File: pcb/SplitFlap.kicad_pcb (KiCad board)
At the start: 2 copper layers, 35 x 35 mm, 21 parts, among them J1 A1_3, U1 PCF8575DBR, U2 ULN2003

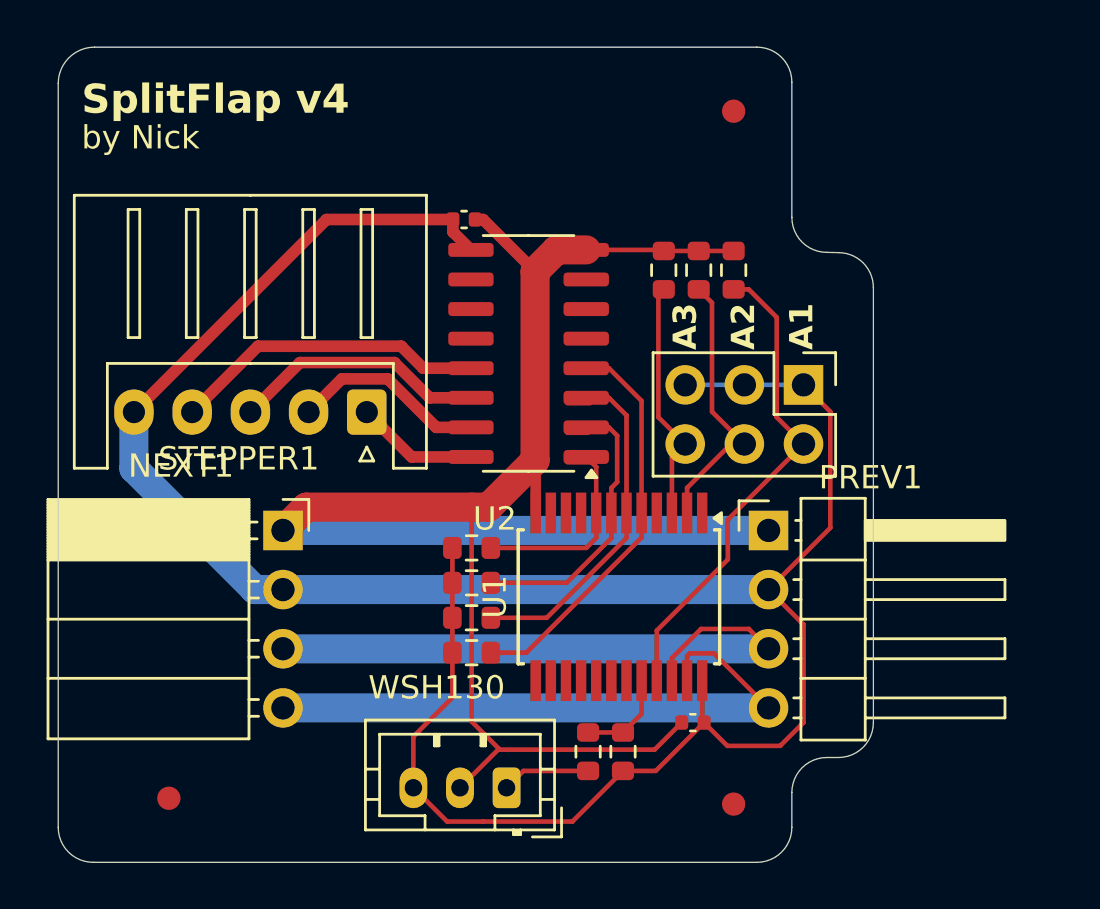
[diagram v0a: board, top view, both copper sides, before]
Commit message: Add optional data lines pull-up
Required as the ESP32 by default does not pull up the data lines to
5v.  Should only be activated once per circuit (display).
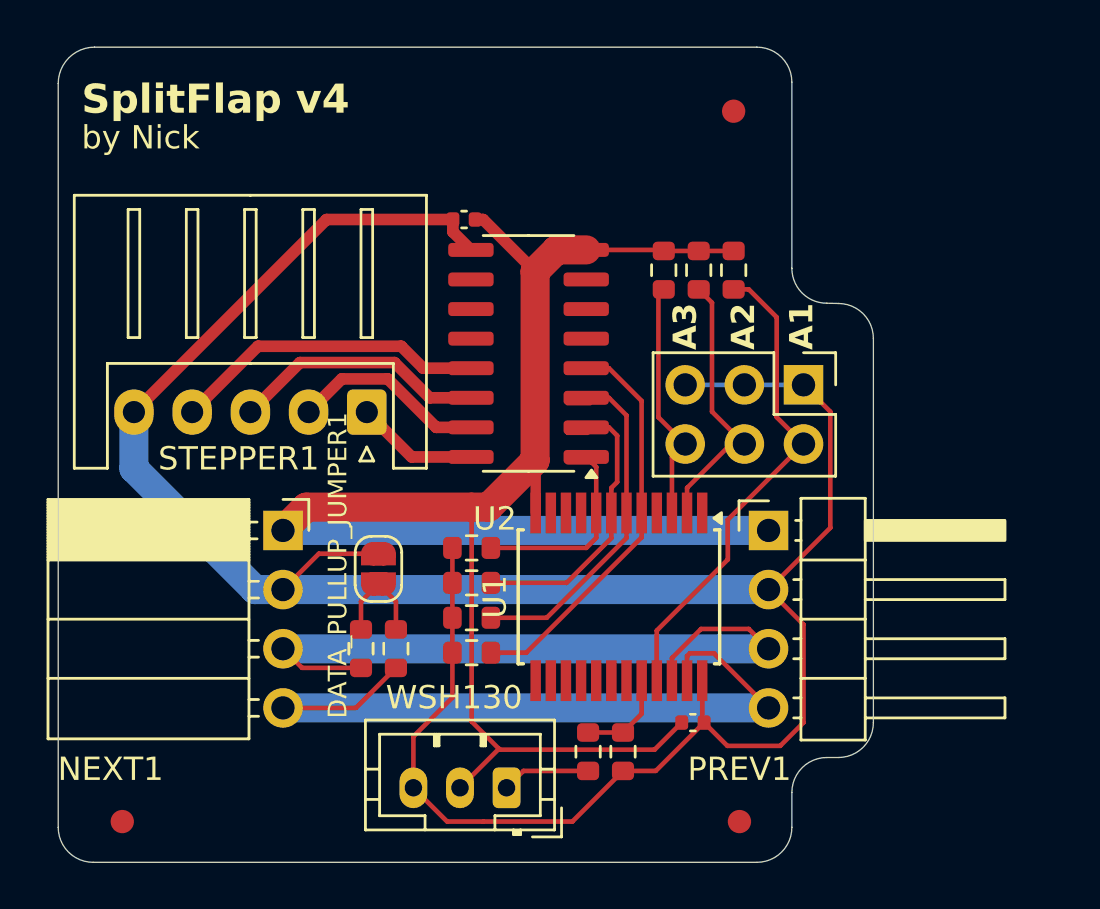
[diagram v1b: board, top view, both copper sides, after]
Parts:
- added DATA_PULLUP_JUMPER1: SolderJumper_2_Open, Jumper:SolderJumper-2_P1.3mm_Open_RoundedPad1.0x1.5mm, F.Cu at (158.8, 81.9)
- added SCL_PULL_UP1: 4K7, Resistor_SMD:R_0603_1608Metric, F.Cu at (158.0, 85.3)
- added SDA_PULL_UP1: 4K7, Resistor_SMD:R_0603_1608Metric, F.Cu at (159.5, 85.3)
- moved REF** 2.24 mm to (147.8, 92.8)
- moved REF** 0.79 mm to (174.2, 92.8)
- renumbered C1 to C1_BYPASS1
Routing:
- net Net-(NEXT1-Pin_4): track 26.4 -> 32.0 mm
- net +5V: track 105.1 -> 109.9 mm
- net Net-(DATA_PULLUP_JUMPER1-B): track 0.00 -> 4.52 mm
- net Net-(NEXT1-Pin_3): track 26.8 -> 30.5 mm
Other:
- outline, holes or cut-outs redrawn

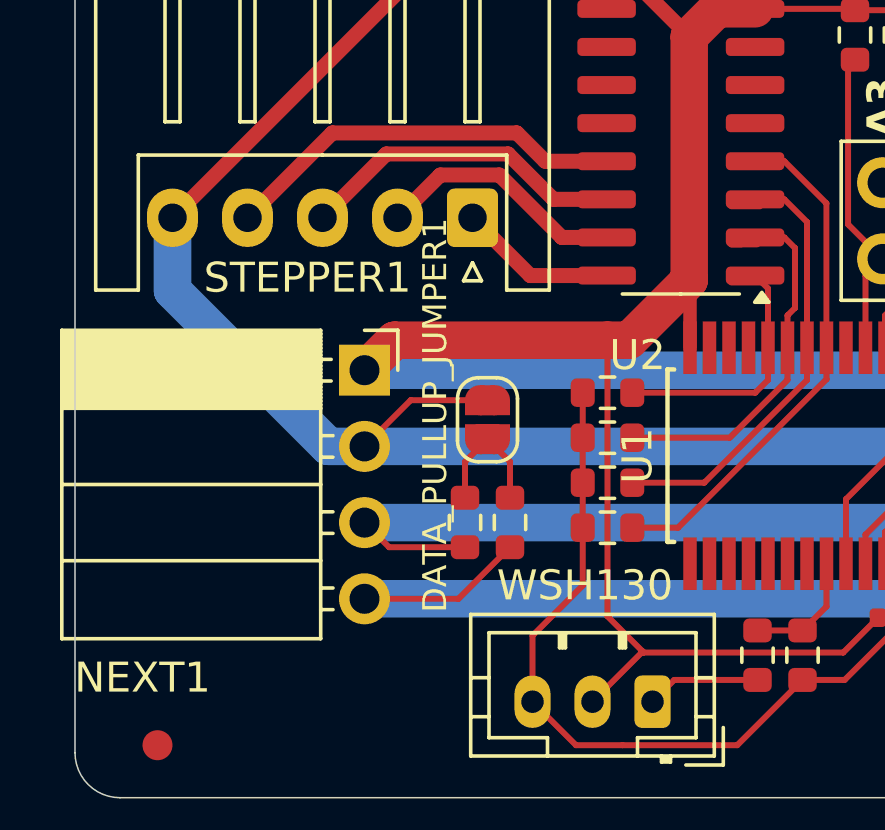
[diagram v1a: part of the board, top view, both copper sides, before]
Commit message: Rename pull-up jumper
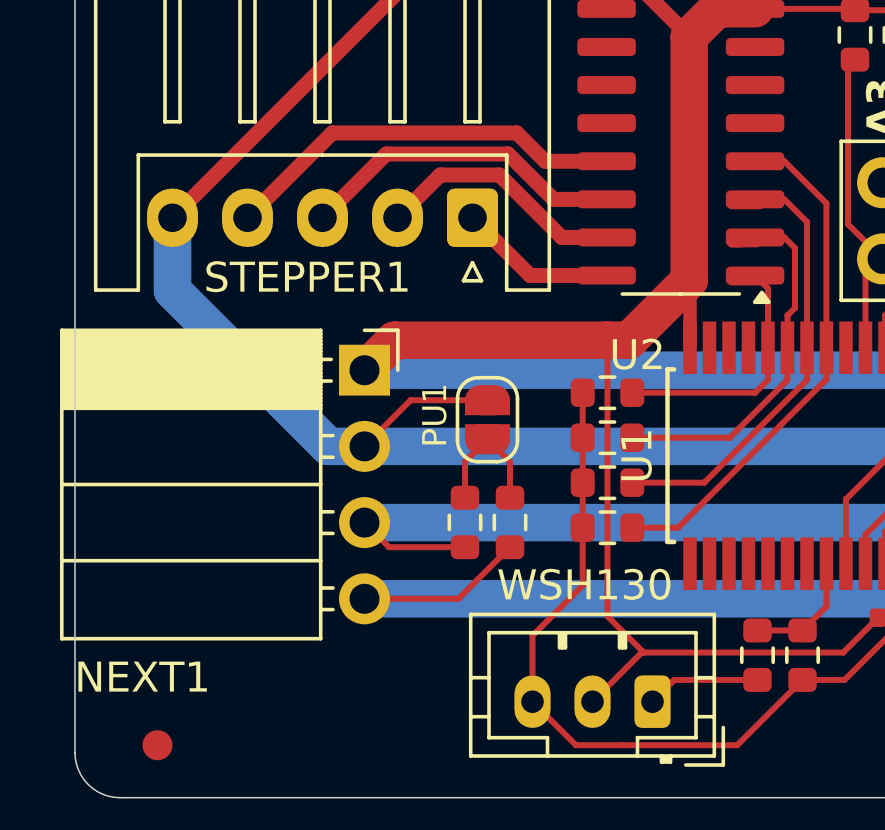
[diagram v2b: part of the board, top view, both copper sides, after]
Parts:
- renumbered DATA_PULLUP_JUMPER1 to PU1
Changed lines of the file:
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@@
 		(descr "SMD Solder Jumper, 1x1.5mm, rounded Pads, 0.3mm gap, open")
 		(tags "solder jumper open")
-		(property "Reference" "DATA_PULLUP_JUMPER1"
+		(property "Reference" "PU1"
 			(at -0.15 1.75 90)
 			(layer "F.SilkS")

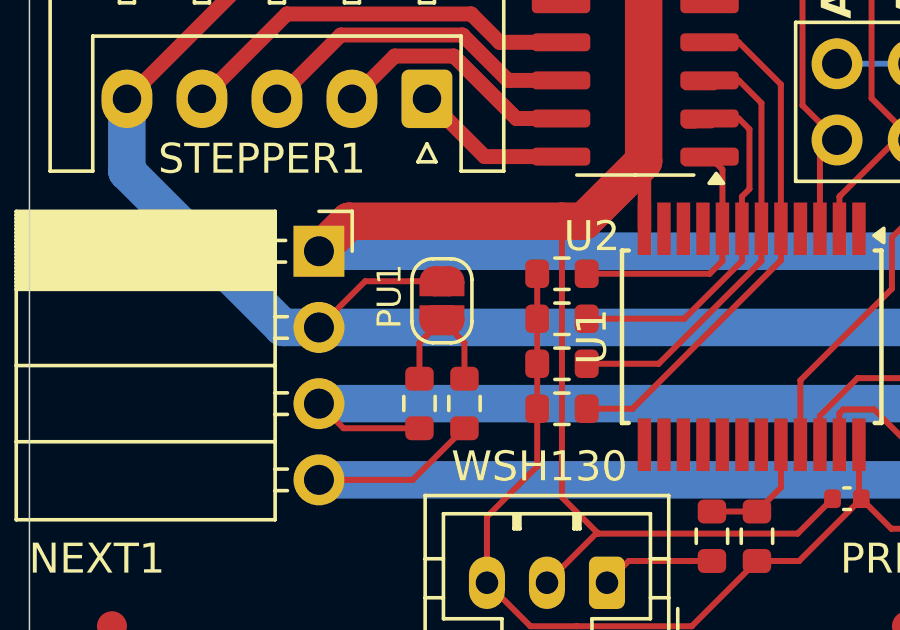
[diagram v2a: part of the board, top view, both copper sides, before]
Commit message: Fix floating pull-ups
The optional pull-ups added in v4 added an unintentional floating node
that would tie SCL and SDA together whenever the pull-up pad was
unsoldered.  Causing the I2C bus to fail (surprisingly only after
connecting 3 modules).
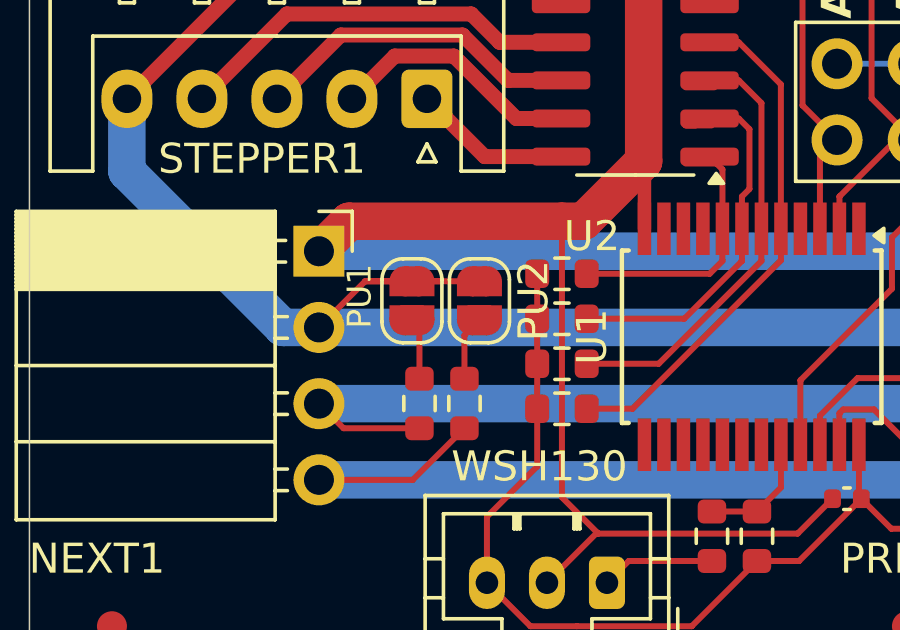
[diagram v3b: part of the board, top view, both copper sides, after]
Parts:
- added PU2: SolderJumper_2_Open, Jumper:SolderJumper-2_P1.3mm_Open_RoundedPad1.0x1.5mm, F.Cu at (160.0, 81.9)
- PULL_UP6, PULL_UP7, PULL_UP8, PULL_UP9: value 2k2 -> 10k
- moved PU1 1.00 mm to (157.8, 81.9)
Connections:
- PU1 pad 2: Net-(DATA_PULLUP_JUMPER1-B) -> Net-(PU1-B)
- SCL_PULL_UP1 pad 1: Net-(DATA_PULLUP_JUMPER1-B) -> Net-(PU1-B)
- SDA_PULL_UP1 pad 1: Net-(DATA_PULLUP_JUMPER1-B) -> Net-(PU2-B)
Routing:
- net Net-(DATA_PULLUP_JUMPER1-B): track 4.52 -> 0.00 mm
- net +5V: track 109.9 -> 113.7 mm
- net Net-(PU2-B): track 0.00 -> 2.16 mm
- net Net-(PU1-B): track 0.00 -> 2.05 mm

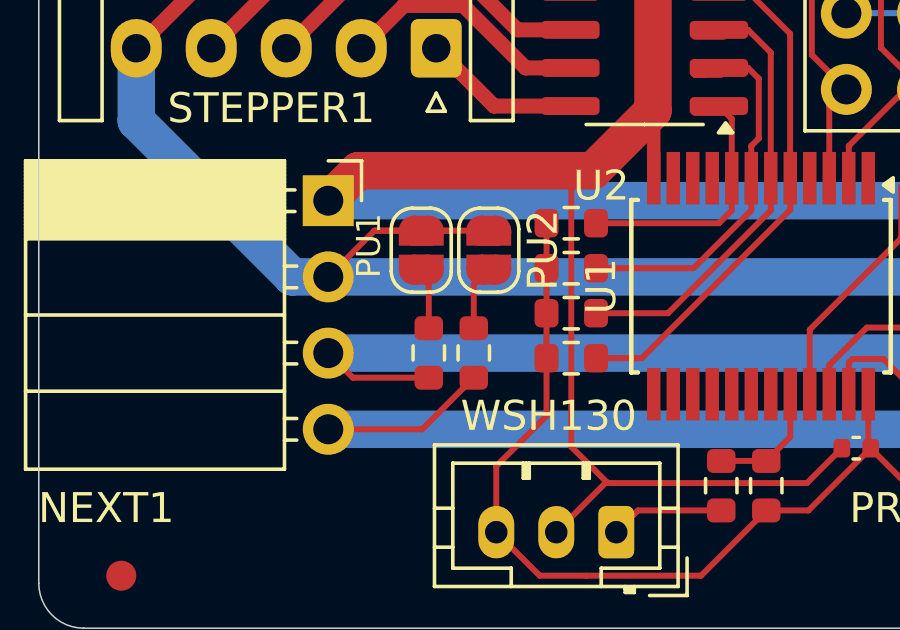
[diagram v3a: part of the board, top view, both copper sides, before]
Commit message: Remove pull-ups entirely
For now manually soldering pull-ups to the ESP32 remain an easier solution.
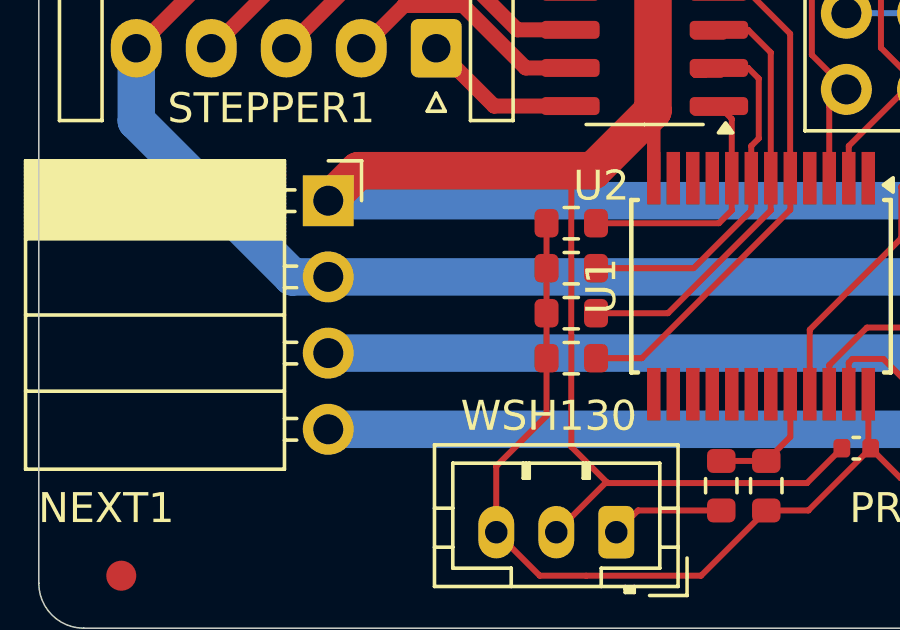
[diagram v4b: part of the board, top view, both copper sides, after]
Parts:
- removed PU1, PU2: SolderJumper_2_Open, Jumper:SolderJumper-2_P1.3mm_Open_RoundedPad1.0x1.5mm
- removed SCL_PULL_UP1, SDA_PULL_UP1: 4K7, Resistor_SMD:R_0603_1608Metric
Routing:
- net +5V: track 113.7 -> 105.1 mm
- net Net-(NEXT1-Pin_4): track 32.0 -> 26.4 mm
- net Net-(NEXT1-Pin_3): track 30.5 -> 26.8 mm
- net Net-(PU2-B): track 2.16 -> 0.00 mm
- net Net-(PU1-B): track 2.05 -> 0.00 mm
